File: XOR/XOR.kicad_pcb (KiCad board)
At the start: 2 copper layers, 20 x 22.5 mm, 9 parts, among them J1 AudioJack2_SwitchT, J2 AudioJack2_SwitchT, J3 AudioJack2_SwitchT, Q1 BSS84, Q2 BSS84, Q3 BSS84, Q4 BSS84, Q5 BSS84, Q6 BSS84

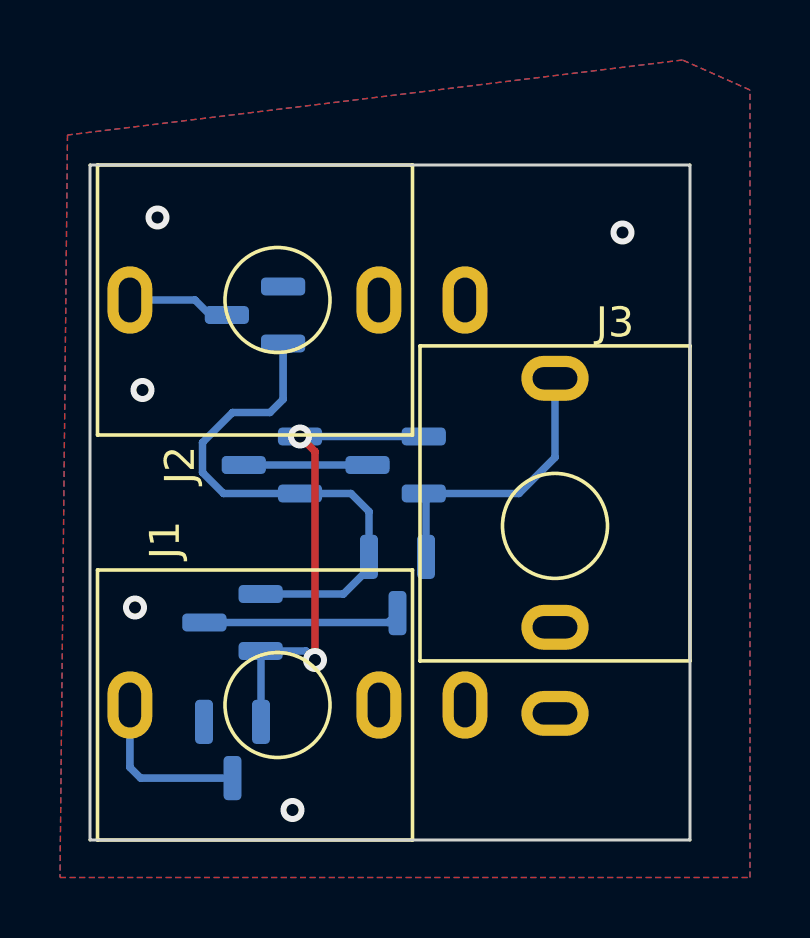
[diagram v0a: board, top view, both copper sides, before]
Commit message: Add XOR gate front panel
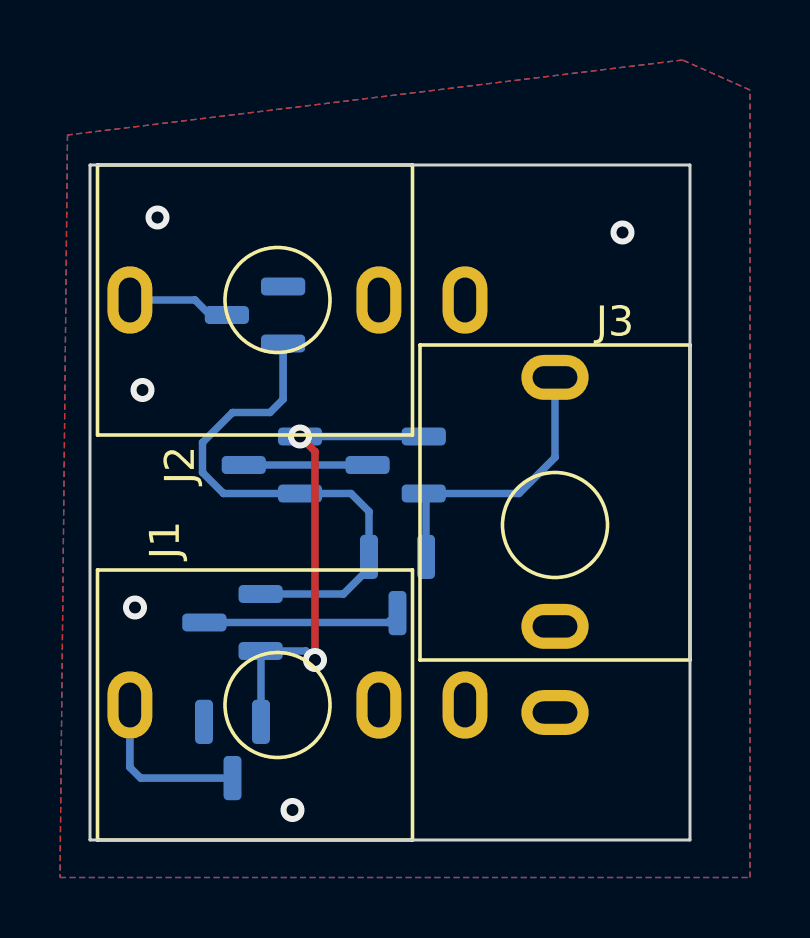
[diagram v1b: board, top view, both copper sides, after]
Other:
- board text added: "Passive XOR"
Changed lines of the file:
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@@
 	(footprint "Custom_FP:PJ398SM"
 		(layer "F.Cu")
-		(at 165.5 87.03)
+		(at 165.5 87)
 		(property "Reference" "J3"
 			(at 2 -6.78 0)
@@
 		(layer "Edge.Cuts")
 	)
+	(gr_text "Passive\nXOR"
+		(at 166.2 79.45 0)
+		(layer "B.SilkS")
+		(effects
+			(font
+				(size 1 1)
+				(thickness 0.15)
+			)
+			(justify bottom mirror)
+		)
+	)
 	(via

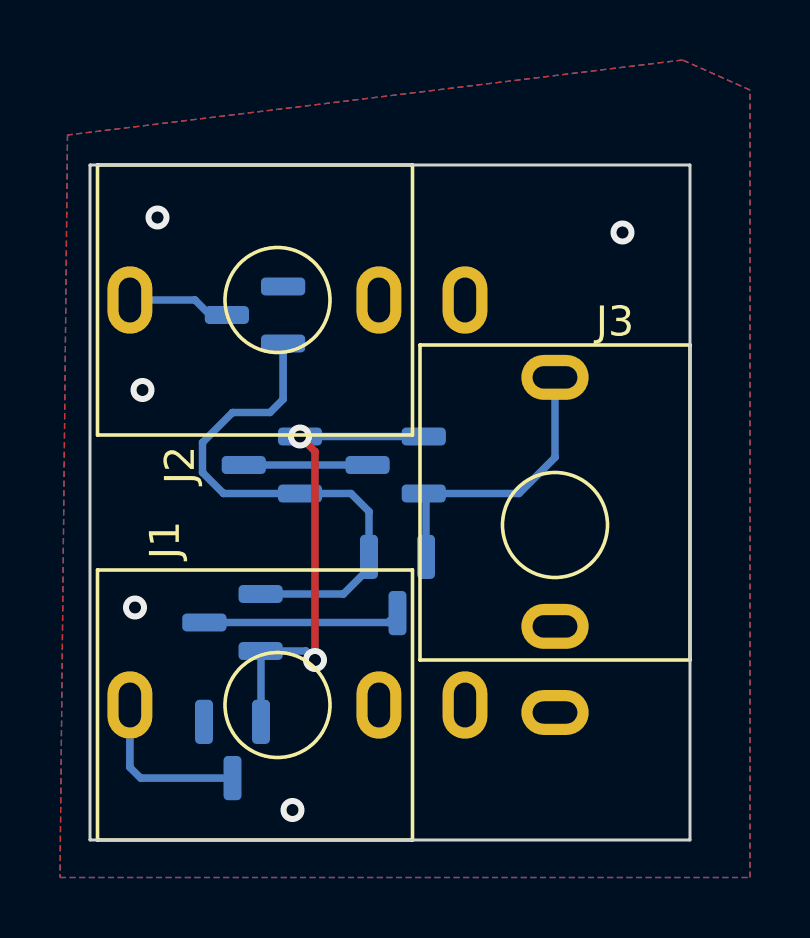
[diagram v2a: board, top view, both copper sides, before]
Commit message: Add pulldown when XOR inputs are high
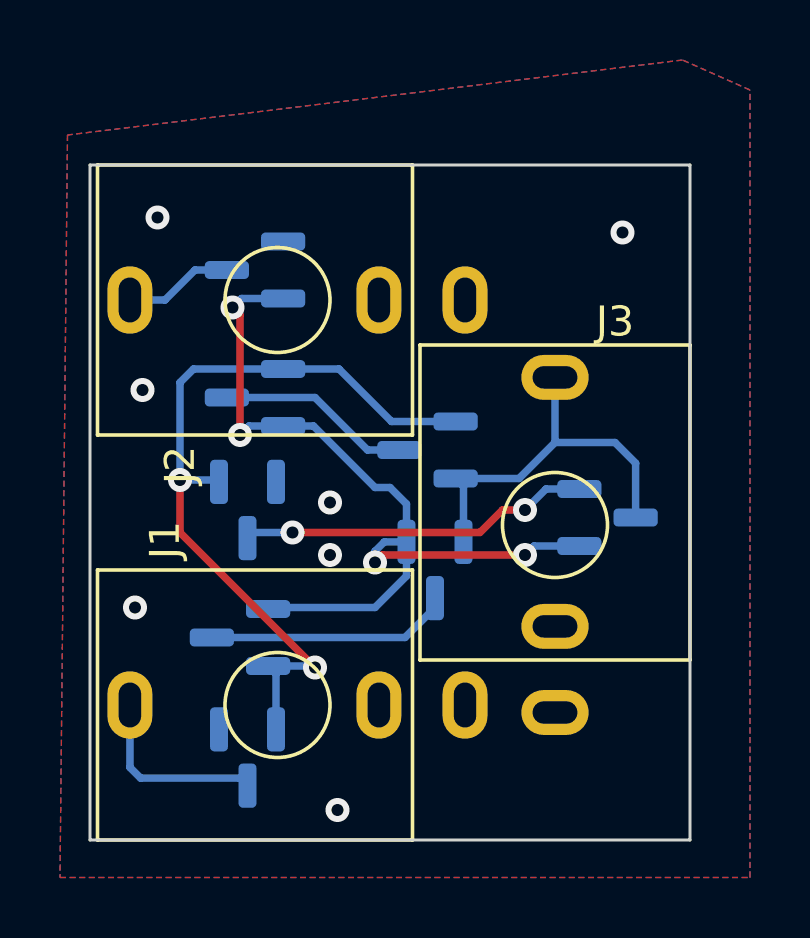
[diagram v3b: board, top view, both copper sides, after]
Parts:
- added Q7: 2N7002, Package_TO_SOT_SMD:SOT-23, B.Cu at (167.2, 86.8)
- added Q8: 2N7002, Package_TO_SOT_SMD:SOT-23, B.Cu at (155.2, 86.5)
- moved Q5 2.32 mm to (155.5, 82.8)
- moved Q6 1.50 mm to (155.5, 78.5)
- moved Q3 1.35 mm to (161.5, 88.5)
- moved Q4 1.17 mm to (161.2, 84.5)
- moved Q1 0.56 mm to (155.2, 94.8)
- moved Q2 0.56 mm to (155.0, 90.8)
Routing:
- net Net-(Q7-S): track 0.00 -> 11.7 mm, vias 0 -> 2
- net Net-(Q2-G): track 18.1 -> 29.0 mm, vias 0 -> 4
- net Net-(Q1-S): track 16.1 -> 26.6 mm
- net Net-(Q3-S): track 9.66 -> 13.0 mm
- net Net-(Q4-D): track 4.12 -> 6.47 mm
- net Net-(Q2-D): track 6.57 -> 8.16 mm
- net Net-(Q1-D): track 5.65 -> 6.25 mm
- net GND: vias 5 -> 7
